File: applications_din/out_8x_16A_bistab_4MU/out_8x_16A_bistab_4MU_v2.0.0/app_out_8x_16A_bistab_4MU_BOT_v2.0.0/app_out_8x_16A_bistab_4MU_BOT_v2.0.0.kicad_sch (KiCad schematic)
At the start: 30 parts, among them IC1 ULN2803, IC2 ULN2803, K1 HFE20-1-024-1HD504, K2 HFE20-1-024-1HD504, K3 HFE20-1-024-1HD504, K4 HFE20-1-024-1HD504, K5 HFE20-1-024-1HD504, K6 HFE20-1-024-1HD504, K7 HFE20-1-024-1HD504, K8 HFE20-1-024-1HD504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

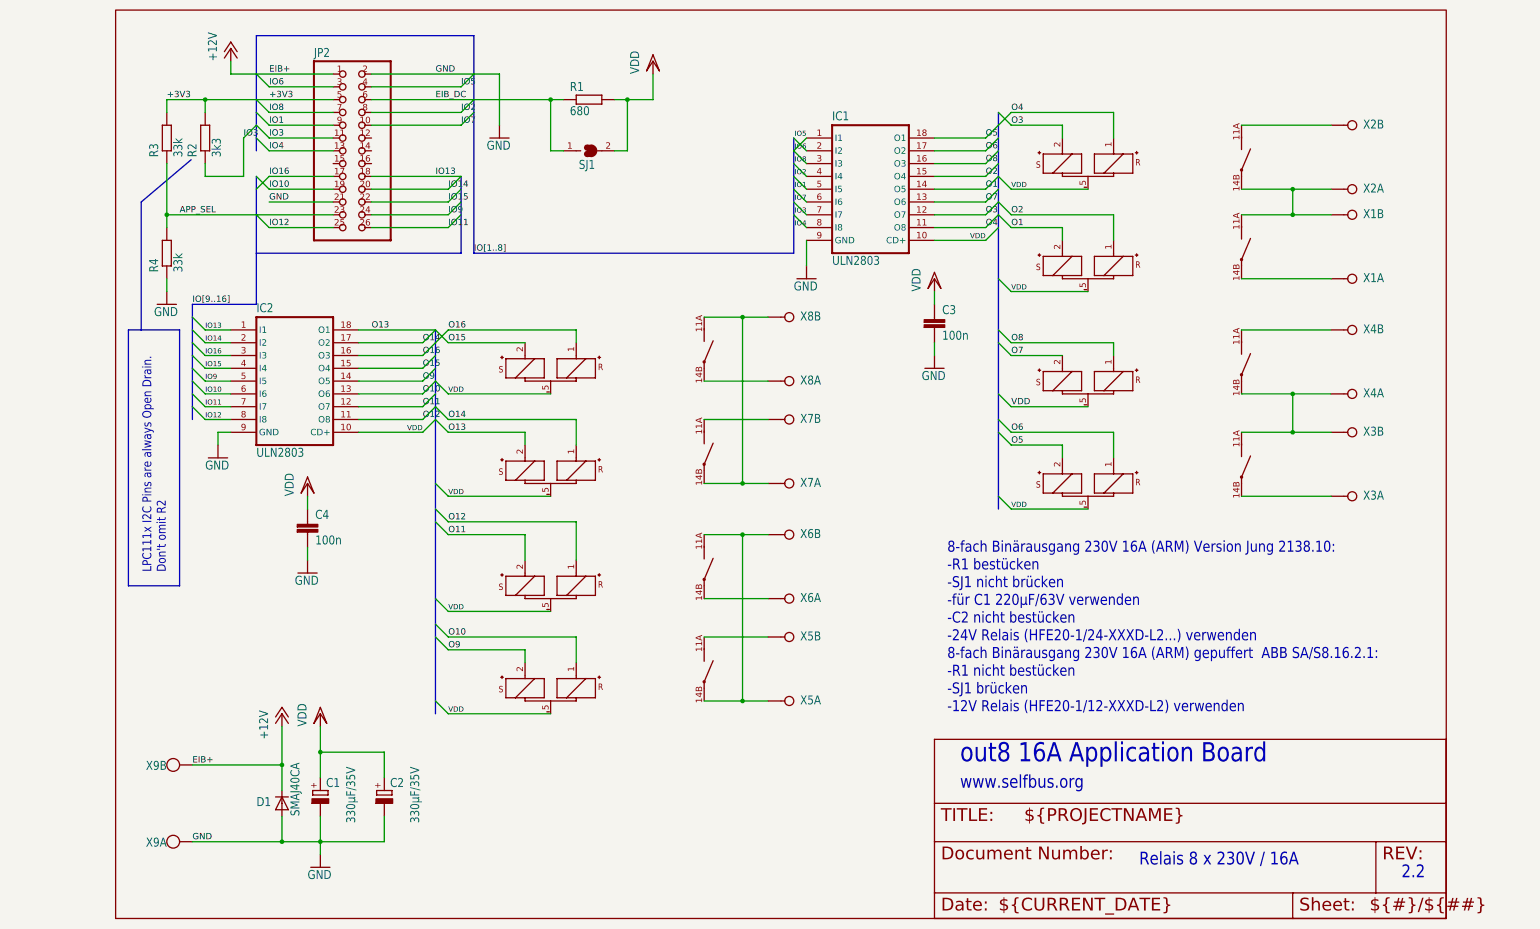
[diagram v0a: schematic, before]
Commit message: properly rename 4in-2out application & top projects
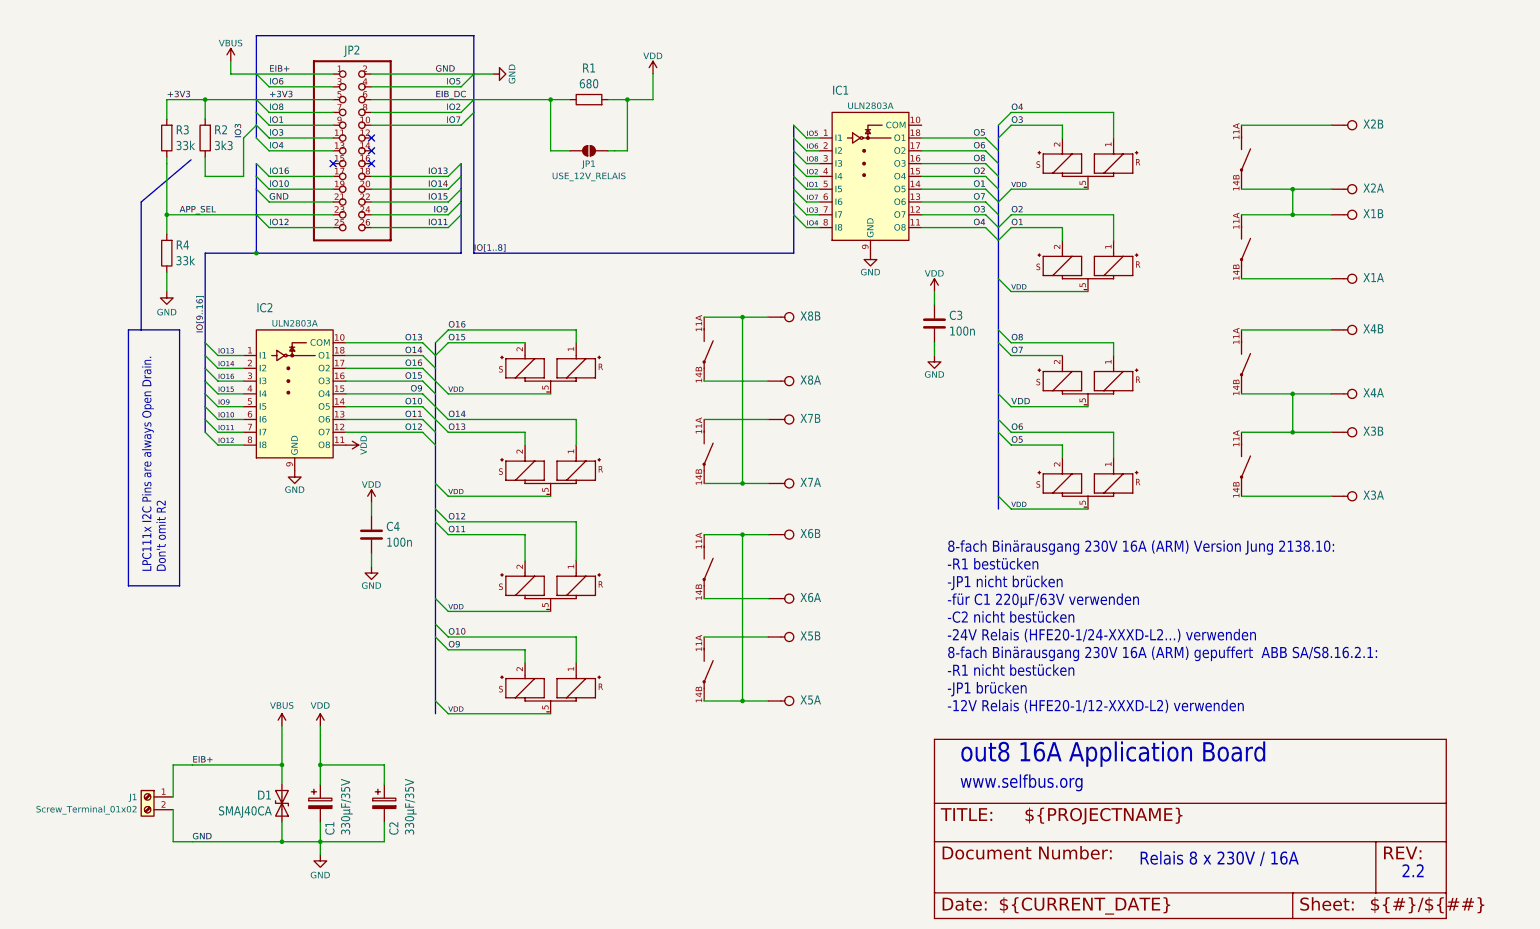
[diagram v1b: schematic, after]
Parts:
- removed X9: W237-102, app_out_8x_16A_bistab_4MU_BOT_v2.0.0:W237-102, symbol app_out_8x_16A_bistab_4MU_BOT_v2.0.0-eagle-import:W237-102
- added J1: Screw_Terminal_01x02, symbol Connector:Screw_Terminal_01x02
- C1, C2: symbol app_out_8x_16A_bistab_4MU_BOT_v2.0.0-eagle-import:CPOL-EUE3.5-8 -> Device:C_Polarized
- C3, C4: symbol app_out_8x_16A_bistab_4MU_BOT_v2.0.0-eagle-import:C-EUC1206 -> Device:C
- D1: footprint app_out_8x_16A_bistab_4MU_BOT_v2.0.0:SMB -> Diode_SMD:D_SMA; symbol app_out_8x_16A_bistab_4MU_BOT_v2.0.0-eagle-import:D-SMB -> Diode:SMAJ40CA
- IC1, IC2: value ULN2803 -> ULN2803A; symbol app_out_8x_16A_bistab_4MU_BOT_v2.0.0-eagle-import:ULN2803ASOP18 -> Transistor_Array:ULN2803A
- JP1: renamed from SJ1; value A -> USE_12V_RELAIS; symbol app_out_8x_16A_bistab_4MU_BOT_v2.0.0-eagle-import:SJ -> Jumper:SolderJumper_2_Open; now left out of the parts list
- R1, R2, R3, R4: symbol app_out_8x_16A_bistab_4MU_BOT_v2.0.0-eagle-import:R-EU_M1206 -> Device:R
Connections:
- net GND: now also C1.2, C2.2, D1.1 (A1), J1.2 (Pin_2); no longer C1.-, C2.-, D1.2 (A)
- net O10: now also IC2.14 (O5); no longer IC2.13 (O6)
- net O11: now also IC2.13 (O6); no longer IC2.12 (O7)
- net O12: now also IC2.12 (O7); no longer IC2.11 (O8)
- net O13: now also IC2.10 (COM); no longer IC2.18 (O1)
- net O14: now also IC2.18 (O1); no longer IC2.17 (O2)
- net O15: now also IC2.16 (O3); no longer IC2.15 (O4)
- net O16: now also IC2.17 (O2); no longer IC2.16 (O3)
- net O9: now also IC2.15 (O4); no longer IC2.14 (O5)
- net VDD: now also C1.1, C2.1, IC2.11 (O8); no longer C1.+, C2.+, IC1.10 (CD+), IC2.10 (CD+)
- net +12V renamed VBUS
- net VBUS: now also D1.2 (A2), J1.1 (Pin_1); no longer D1.1 (C)
- no-connect marks 0 -> 4
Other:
- note added: "8-fach Binärausgang 230V 16A (ARM) Version Jung 2138.10: -R1 bestücken -JP1 nicht brücken -für C1 220µF/63V verwenden -C2 nicht bestücken -24V Relais (HFE20-1/24-XXXD-L2...) verwenden 8-fach Binärausgang 230V 16A (ARM) gepuffert ABB SA/S8.16.2.1: -R1 nicht bestücken -JP1 brücken -12V Relais (HFE20-1/12-XXXD-L2) verwenden"
- note removed: "8-fach Binärausgang 230V 16A (ARM) Version Jung 2138.10: -R1 bestücken -SJ1 nicht brücken -für C1 220µF/63V verwenden -C2 nicht bestücken -24V Relais (HFE20-1/24-XXXD-L2...) verwenden 8-fach Binärausgang 230V 16A (ARM) gepuffert ABB SA/S8.16.2.1: -R1 nicht bestücken -SJ1 brücken -12V Relais (HFE20-1/12-XXXD-L2) verwenden"
- moved on the sheet: JP1
